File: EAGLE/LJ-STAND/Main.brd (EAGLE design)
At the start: 158.5 x 133.6 mm, 129 parts

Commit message: Main pcb
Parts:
- removed MTR1_OUT_RIGHT, MTR2_OUT_LEFT, MTR3_OUT_BACKRIGHT, MTR4_OUT_BACKLEFT: PH, adafruit:JST-PH-2-SMT
- added BACKLEFT, BACKRIGHT, LEFT, RIGHT: PH, adafruit:JST-PH-2-THM
- added SONAR: (no value), SparkFun-Connectors:1X04
- C14: value 10uF Tantalum -> 10uF
- LIGHT_GATE: device SparkFun-Connectors:1X04 -> SparkFun-Connectors:1X05
- moved 9 317.2 mm to (193.0, 63.2)
- moved 8 311.8 mm to (200.8, 77.5)
- moved R8 308.5 mm to (213.0, 104.0)
- moved 7 307.6 mm to (209.2, 91.4)
- moved 6 305.3 mm to (218.9, 107.5)
- moved R7 304.5 mm to (213.1, 106.7)
- moved LIGHT_GATE 302.3 mm to (133.5, 153.8), turned to 180 degrees
- moved R6 300.4 mm to (213.2, 112.1)
- moved R5 296.2 mm to (213.0, 114.8)
- moved C4 288.7 mm to (162.4, 166.7), turned to 165 degrees
- moved SDA 288.3 mm to (209.1, 113.2)
- moved C54 287.1 mm to (163.8, 109.3)
- moved 5 284.5 mm to (209.3, 123.8)
- moved R2 282.3 mm to (209.2, 101.5)
- moved SCL 280.0 mm to (209.1, 105.0)
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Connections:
- net +5V: now also SONAR.1
- net GND: now also LIGHT_GATE.5, SONAR.4
- net N$1: now also LEFT.1; no longer MTR2_OUT_LEFT.1
- net N$14: now also BACKRIGHT.1; no longer MTR3_OUT_BACKRIGHT.1
- net N$16: now also BACKRIGHT.2; no longer MTR3_OUT_BACKRIGHT.2
- net N$2: now also LEFT.2; no longer MTR2_OUT_LEFT.2
- net N$22: now also BACKLEFT.1; no longer MTR4_OUT_BACKLEFT.1
- net N$26: now also BACKLEFT.2; no longer MTR4_OUT_BACKLEFT.2
- net N$5: now also RIGHT.1; no longer MTR1_OUT_RIGHT.1
- net N$7: now also RIGHT.2; no longer MTR1_OUT_RIGHT.2
- net SCL_5V: now also SONAR.3
- net SDA_5V: now also SONAR.2
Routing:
- net TSOP_PWR: track 0.00 -> 74.9 mm
- net +3V3: track 0.00 -> 6.44 mm
- added copper zone on layer 16, net GND
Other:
- outline, holes or cut-outs redrawn
- board text added: "1"

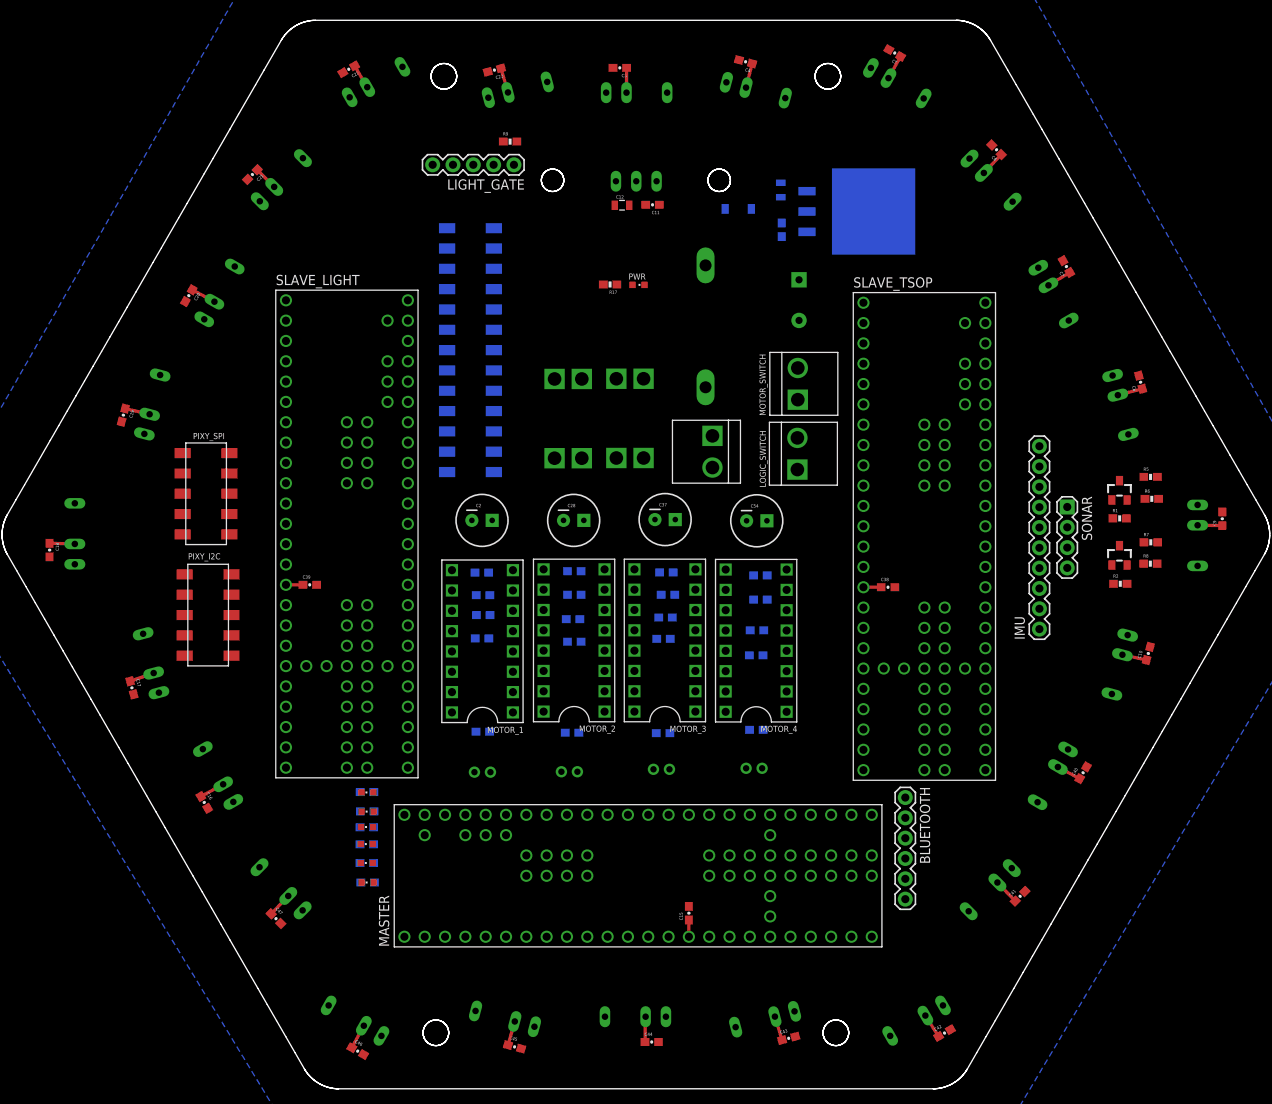
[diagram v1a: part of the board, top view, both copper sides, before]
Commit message: new top plate
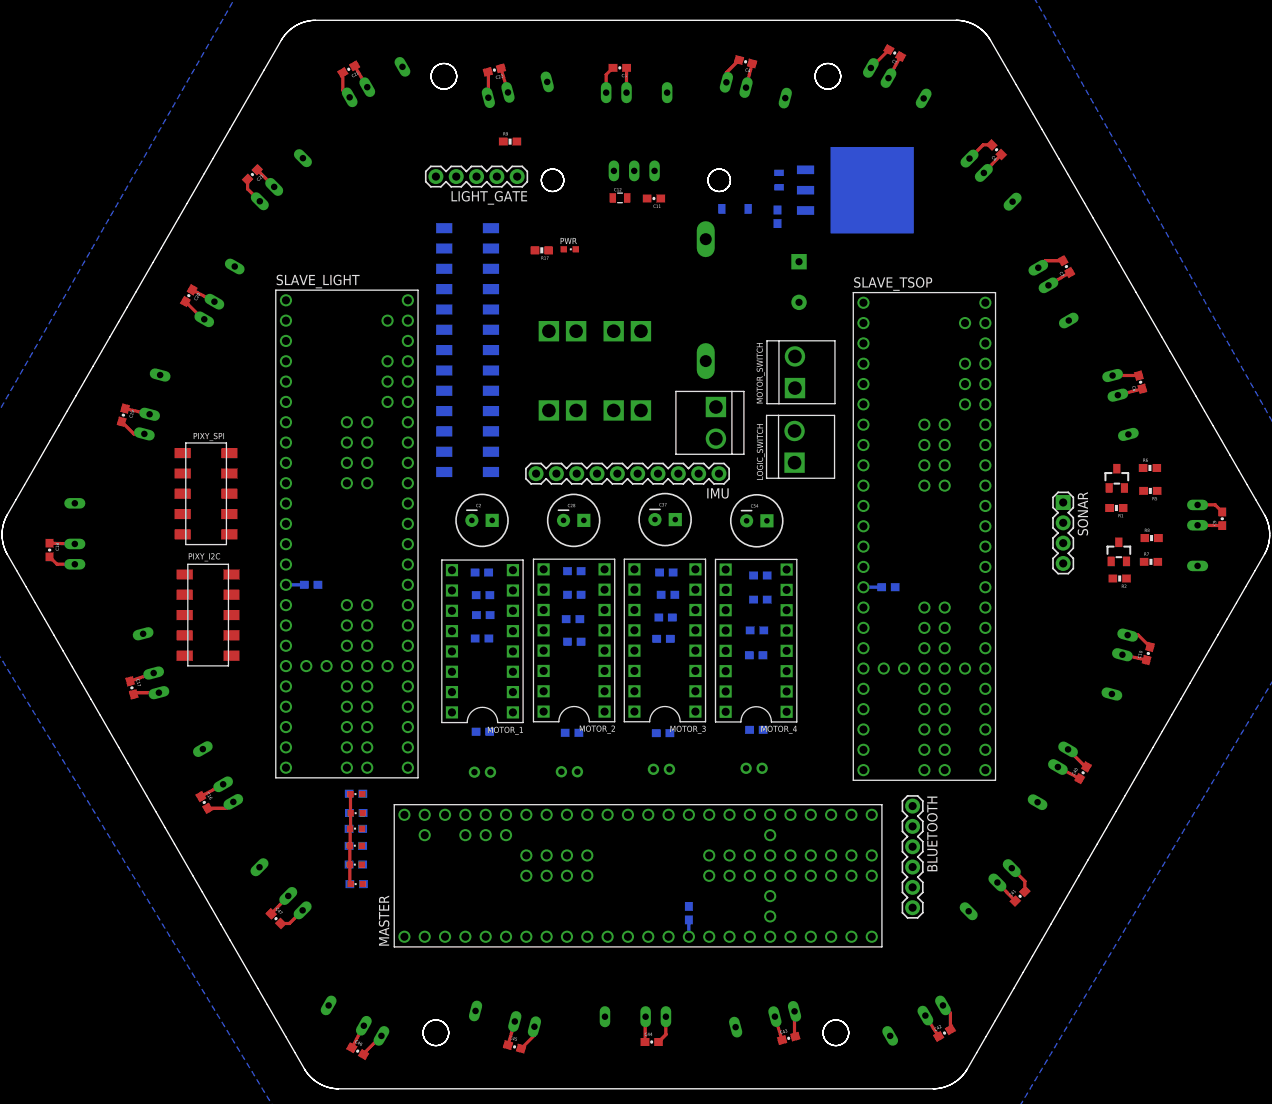
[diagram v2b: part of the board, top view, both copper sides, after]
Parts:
- moved IMU 44.5 mm to (159.1, 115.2), turned to 180 degrees
- moved PWR 9.67 mm to (140.4, 143.3)
- moved R17 9.54 mm to (136.9, 143.2)
- moved LOGIC_FUSE 6.01 mm to (141.2, 133.0)
- moved MOTOR_FUSE 5.95 mm to (149.3, 133.0)
- moved R6 3.87 mm to (213.0, 116.0)
- moved PWR_IN 3.63 mm to (158.7, 121.6)
- moved D1 3.28 mm to (157.4, 136.9)
- moved R8 3.20 mm to (213.2, 107.2)
- moved VREG-3.3V 2.67 mm to (175.7, 150.7)
- moved R7 2.44 mm to (213.1, 104.2)
- moved C1 2.26 mm to (169.1, 139.2)
- moved R5 1.75 mm to (213.0, 113.1), turned to 180 degrees
- moved C13 1.71 mm to (166.4, 147.3)
- moved SDA 1.53 mm to (208.8, 114.7)
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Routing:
- net GND: track 0.00 -> 92.7 mm

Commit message: Main pcb
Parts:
- moved D2 8.44 mm to (159.3, 156.6)
- moved SONAR 3.49 mm to (205.3, 113.1)
- moved R8 1.81 mm to (214.1, 108.7)
- moved SCL 1.68 mm to (209.4, 107.1)
- moved R5 1.30 mm to (214.1, 112.5)
- moved R7 1.16 mm to (214.1, 104.8)
- moved R6 1.16 mm to (214.1, 115.8)
- moved R2 1.09 mm to (209.5, 103.2)
- moved SDA 1.04 mm to (209.8, 114.9)
- moved C14 0.94 mm to (165.9, 152.5)
- moved R1 0.74 mm to (209.5, 110.7)
- moved C1 0.60 mm to (168.7, 138.7)
- moved VREG-3.3V 0.54 mm to (175.2, 150.6)
- moved C13 0.27 mm to (166.1, 147.4)
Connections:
- removed net N$37: LIGHT_GATE.1
- net +5V: now also LIGHT_GATE.1
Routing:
- net TSOP_PWR: track 74.9 -> 593.4 mm
- net TSOP17: track 0.00 -> 254.8 mm, vias 0 -> 3
- net TSOP16: track 0.00 -> 228.8 mm, vias 0 -> 3
- net TSOP15: track 0.00 -> 204.8 mm, vias 0 -> 3
- net TSOP14: track 0.00 -> 175.8 mm, vias 0 -> 1
- net TSOP13: track 0.00 -> 151.8 mm, vias 0 -> 1
- net TSOP12: track 0.00 -> 131.3 mm, vias 0 -> 1
- net TSOP11: track 0.00 -> 111.3 mm, vias 0 -> 1
- net TSOP9: track 0.00 -> 104.6 mm
- net TSOP8: track 0.00 -> 88.2 mm
- net TSOP7: track 0.00 -> 73.3 mm
- net TSOP10: track 0.00 -> 73.3 mm
- net TSOP5: track 0.00 -> 59.2 mm
- net TSOP6: track 0.00 -> 55.3 mm
- net TSOP4: track 0.00 -> 42.1 mm
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
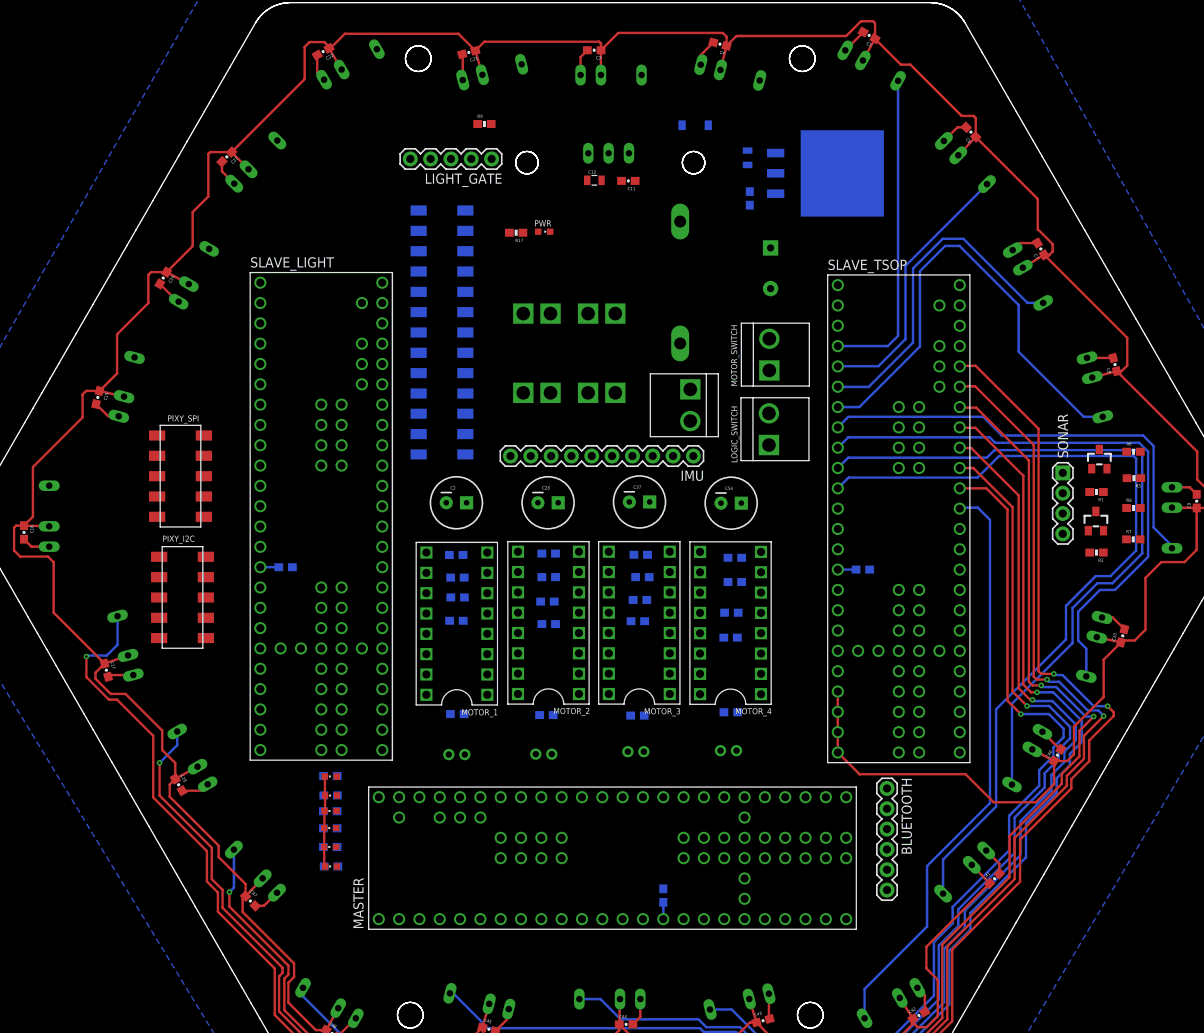
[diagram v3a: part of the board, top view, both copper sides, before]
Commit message: More main pcb routing
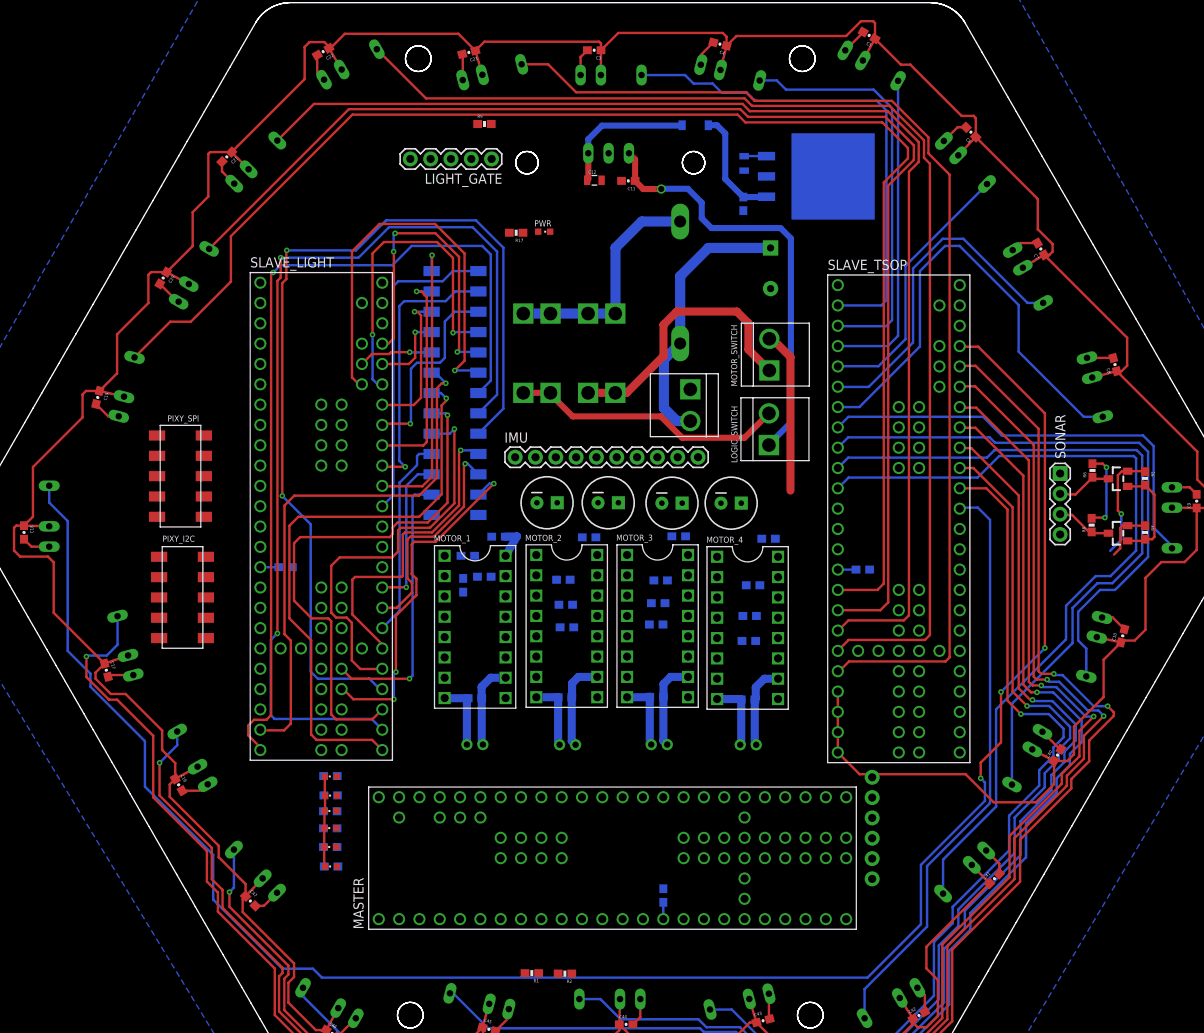
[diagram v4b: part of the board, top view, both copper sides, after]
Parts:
- moved R1 92.7 mm to (138.9, 50.6)
- moved R2 84.8 mm to (143.0, 50.5)
- moved IMU 22.3 mm to (136.8, 115.1), turned to 0 degrees
- moved BLUETOOTH 11.5 mm to (181.4, 62.4), flipped to the bottom, turned to 90 degrees
- moved C2 11.3 mm to (140.8, 109.4)
- moved LIGHT_SENSOR_CONNECTOR 7.74 mm to (129.3, 123.1), turned to 270 degrees
- moved C28 7.52 mm to (148.4, 109.4)
- moved C53 5.76 mm to (134.7, 105.2), turned to 180 degrees
- moved R8 5.65 mm to (208.9, 106.6), turned to 90 degrees
- moved R6 5.64 mm to (209.0, 113.4), turned to 90 degrees
- moved C33 5.45 mm to (146.1, 105.1), turned to 180 degrees
- moved C26 5.36 mm to (130.9, 102.8), turned to 180 degrees
- moved C52 5.28 mm to (157.3, 105.2), turned to 180 degrees
- moved C56 4.85 mm to (168.5, 104.9), turned to 180 degrees
- moved C25 4.52 mm to (130.3, 99.1), turned to 90 degrees
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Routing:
- net TSOP18: track 0.00 -> 240.3 mm, vias 0 -> 3
- net TSOP19: track 0.00 -> 176.1 mm
- net TSOP20: track 0.00 -> 162.4 mm
- net TSOP21: track 0.00 -> 153.4 mm
- net TSOP22: track 0.00 -> 147.6 mm
- net TSOP23: track 0.00 -> 135.4 mm
- net LS14: track 0.00 -> 123.5 mm, vias 0 -> 2
- net LS16: track 0.00 -> 118.8 mm, vias 0 -> 2
- net LS12: track 0.00 -> 109.5 mm, vias 0 -> 1
- net LS13: track 0.00 -> 71.9 mm, vias 0 -> 1
- net LS11: track 0.00 -> 67.2 mm, vias 0 -> 1
- net LS15: track 0.00 -> 66.5 mm, vias 0 -> 1
- net TSOP0: track 0.00 -> 62.5 mm
- net N$11: track 0.00 -> 54.4 mm, vias 0 -> 1
- net LS10: track 0.00 -> 52.6 mm, vias 0 -> 1
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
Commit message: More routing
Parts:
- moved R18 72.9 mm to (185.6, 63.2), turned to 180 degrees
- moved LED1 72.8 mm to (185.6, 63.2), turned to 270 degrees
- moved LED6 72.6 mm to (185.6, 74.5), turned to 270 degrees
- moved R4 72.6 mm to (185.6, 74.5), turned to 180 degrees
- moved R19 72.2 mm to (185.6, 65.6), turned to 180 degrees
- moved LED5 72.2 mm to (185.7, 72.1), turned to 270 degrees
- moved R3 72.2 mm to (185.7, 72.1), turned to 180 degrees
- moved LED2 72.1 mm to (185.6, 65.6), turned to 270 degrees
- moved R20 72.1 mm to (185.7, 67.6), turned to 180 degrees
- moved LED3 72.0 mm to (185.6, 67.6), turned to 270 degrees
- moved R21 72.0 mm to (185.7, 69.7), turned to 180 degrees
- moved LED4 72.0 mm to (185.7, 69.7), turned to 270 degrees
- moved BLUETOOTH 66.6 mm to (116.1, 75.1), turned to 270 degrees
- moved C50 36.5 mm to (130.2, 98.9), turned to 90 degrees
- moved C51 35.9 mm to (130.9, 102.6), turned to 180 degrees
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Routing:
- net +3V3: track 22.2 -> 252.6 mm, vias 0 -> 6
- net +5V: track 27.6 -> 247.3 mm, vias 2 -> 3
- net LIGHT_GATE: track 0.00 -> 114.1 mm, vias 0 -> 2
- net LED4: track 0.00 -> 76.8 mm, vias 0 -> 1
- net MOTOR_PWR: track 24.7 -> 100.1 mm
- net MTR4_IN1: track 0.00 -> 73.2 mm, vias 0 -> 3
- net MTR4_IN2: track 0.00 -> 72.7 mm, vias 0 -> 2
- net LED3: track 0.00 -> 72.3 mm, vias 0 -> 1
- net MTR4_PWM: track 0.00 -> 69.9 mm, vias 0 -> 2
- net LED2: track 0.00 -> 67.8 mm, vias 0 -> 1
- net LED5: track 0.00 -> 64.1 mm, vias 0 -> 7
- net LED6: track 0.00 -> 63.5 mm, vias 0 -> 6
- net LED1: track 0.00 -> 63.4 mm, vias 0 -> 1
- net MTR3_SB: track 0.00 -> 46.6 mm
- net MTR3_PWM: track 0.00 -> 43.8 mm
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- added copper zone on layer 1, net GND

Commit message: pcb routing
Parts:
- moved PIXY_I2C 1.20 mm to (96.1, 98.4), turned to 90 degrees
- moved PIXY_SPI 1.07 mm to (96.0, 112.9)
- turned LED1 to 90 degrees
- turned LED2 to 90 degrees
- turned LED3 to 90 degrees
- turned LED4 to 90 degrees
- turned LED5 to 90 degrees
- turned LED6 to 90 degrees
- turned R18 to 0 degrees
- turned R19 to 0 degrees
- turned R20 to 0 degrees
- turned R21 to 0 degrees
- turned R3 to 0 degrees
- turned R4 to 0 degrees
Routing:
- net SCL_5V: track 7.03 -> 307.3 mm, vias 0 -> 2
- net SDA_5V: track 7.06 -> 300.2 mm, vias 0 -> 4
- net SDA: track 20.4 -> 284.5 mm, vias 2 -> 12
- net SCK: track 0.00 -> 256.1 mm, vias 0 -> 11
- net SCL: track 9.73 -> 257.1 mm, vias 1 -> 7
- net MISO: track 0.00 -> 235.3 mm, vias 0 -> 12
- net MOSI: track 0.00 -> 224.9 mm, vias 0 -> 11
- net +3V3: track 252.6 -> 463.8 mm, vias 6 -> 19
- net CS_LIGHT: track 0.00 -> 153.7 mm, vias 0 -> 3
- net CS_PIXY: track 0.00 -> 122.4 mm, vias 0 -> 1
- net CS_TSOP: track 0.00 -> 91.8 mm, vias 0 -> 3
- net GND: track 89.4 -> 52.7 mm, vias 0 -> 6
- net BT_TX: track 0.00 -> 14.4 mm
- net +5V: track 247.3 -> 257.1 mm
- net BT_RX: track 0.00 -> 9.70 mm
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
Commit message: Pcb routing done
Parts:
- moved LED2 0.33 mm to (185.8, 65.4)
- moved R19 0.33 mm to (185.8, 65.4)
- moved LED6 0.30 mm to (185.8, 74.3)
- moved R4 0.30 mm to (185.8, 74.3)
- moved LED4 0.20 mm to (185.8, 69.8)
- moved R21 0.20 mm to (185.8, 69.9)
- moved R18 0.19 mm to (185.8, 63.1)
- moved LED1 0.19 mm to (185.8, 63.2)
- moved LED5 0.16 mm to (185.8, 72.1)
- moved R3 0.16 mm to (185.8, 72.1)
- moved LED3 0.13 mm to (185.8, 67.6)
- moved R20 0.13 mm to (185.8, 67.6)
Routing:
- net GND: track 52.7 -> 33.8 mm, vias 6 -> 20
- net N$25: track 0.00 -> 8.40 mm, vias 0 -> 1
- net N$24: track 0.00 -> 8.03 mm, vias 0 -> 1
- net N$33: track 0.00 -> 7.66 mm, vias 0 -> 1
- net N$34: track 0.00 -> 5.85 mm, vias 0 -> 1
- net N$23: track 0.00 -> 4.70 mm, vias 0 -> 1
- net N$29: track 0.00 -> 4.65 mm, vias 0 -> 1
- net MTR1_SB: track 25.6 -> 28.7 mm
- net MTR2_SB: track 26.3 -> 28.9 mm
- net MTR2_PWM: track 18.3 -> 19.9 mm
- net LED3: track 72.1 -> 70.8 mm
- net LED4: track 76.5 -> 75.3 mm
- net LED2: track 67.4 -> 66.2 mm
- net LED6: track 64.1 -> 63.0 mm
- net LED1: track 62.9 -> 61.9 mm
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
